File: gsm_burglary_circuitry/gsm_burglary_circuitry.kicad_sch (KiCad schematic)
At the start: 35 parts, among them U1 ESP32-C6-DevKitC-1, U2 PIR_Sensor, U3 LM2596S-ADJ, U4 PIR_Sensor, U5 HC-SR04_Ultrasonic_Sensor, U6 PIR_Sensor, U7 SIM800L-CORE, U8 LM2596S-ADJ

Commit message: made changes
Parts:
- added BZ1: Buzzer, symbol Device:Buzzer
- added C12: 10uf, Capacitor_THT:CP_Radial_D5.0mm_P2.50mm, symbol PCM_SL_Devices:Capacitor_PO
- added C13: 0.01uf, Capacitor_THT:CP_Radial_D5.0mm_P2.50mm, symbol PCM_SL_Devices:Capacitor_PO
- added Q1: BC547, PCM_Package_TO_SOT_THT_AKL:TO-92_Inline_Wide_CBE, symbol PCM_Transistor_BJT_AKL:BC547
- added R6: 4.7k, PCM_SparkFun-Resistor:R_0603_1608Metric, symbol PCM_SparkFun-Resistor:4.7k_0603
- added R7: 10k, PCM_SparkFun-Resistor:R_0603_1608Metric, symbol PCM_SparkFun-Resistor:4.7k_0603
- added R8: 1k, PCM_SparkFun-Resistor:R_0603_1608Metric, symbol PCM_SparkFun-Resistor:4.7k_0603
- added U9: ICM7555xP, Package_DIP:DIP-8_W7.62mm, symbol Timer:ICM7555xP
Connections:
- net GND: now also C12.2, C13.2, Q1.3 (E), U9.1 (GND)
- net at A1.1 (5V), C10.2, C11.1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: now also BZ1.1 (+), R8.2, U9.8 (VCC)
- net at U1.12 (GPIO2): now also U9.4 (~{RST})
- new net: BZ1.2 (-), Q1.1 (C)
- new net: R6.1, U9.3 (OUT)
- new net: Q1.2 (B), R6.2
- new net: C12.1, R7.1, U9.2 (TRIG), U9.6 (THRES)
- new net: C13.1, U9.5 (CONT)
- new net: R7.2, R8.1

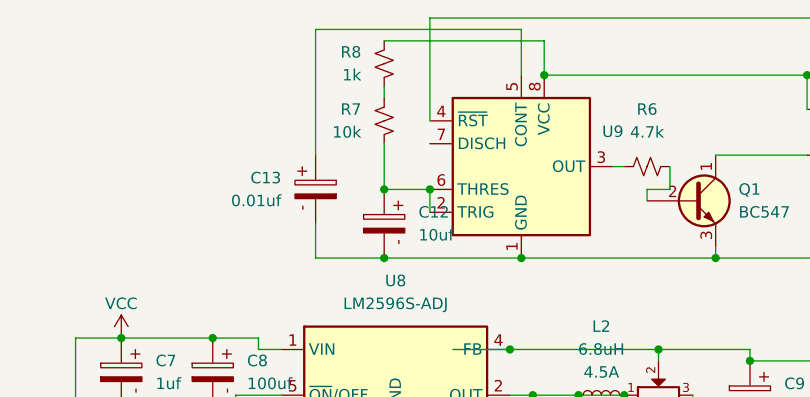
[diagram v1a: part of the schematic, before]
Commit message: feat: Add Buzzer, Resistor, Transistor, and Timer IC symbols to the KiCad schematic.
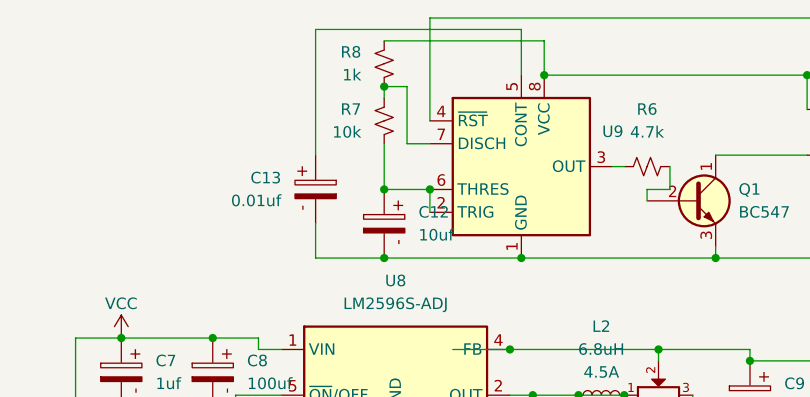
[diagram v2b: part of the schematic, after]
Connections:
- net at U9.7 (DISCH): now also R7.2, R8.1
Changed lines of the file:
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@@
+	)
+	(junction
+		(at 90.17 21.59)
+		(diameter 0)
+		(color 0 0 0 0)
 	)
 	(junction
@@
 	(wire
 		(pts
+			(xy 95.25 27.94) (xy 92.71 27.94)
+		)
+		(stroke
+			(width 0)
+			(type default)
+		)
+	)
+	(wire
+		(pts
 			(xy 119.38 33.02) (xy 119.38 34.29)
 		)
@@
 	(wire
 		(pts
+			(xy 92.71 21.59) (xy 90.17 21.59)
+		)
+		(stroke
+			(width 0)
+			(type default)
+		)
+	)
+	(wire
+		(pts
 			(xy 187.96 63.5) (xy 187.96 88.9)
 		)
@@
 		)
 		(stroke
+			(width 0)
+			(type default)
+		)
+	)
+	(wire
+		(pts
+			(xy 92.71 27.94) (xy 92.71 21.59)
+		)
+		(stroke
